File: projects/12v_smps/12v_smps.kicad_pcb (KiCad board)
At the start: 6 copper layers, 7 parts, among them U2 TPSM82902SISR

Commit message: wip
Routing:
- net /VIN: track 3.07 -> 0.00 mm
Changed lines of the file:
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@@
 		(property ki_fp_filters "R_*")
 		(sheetname "/")
+		(sheetfile "12v_smps.kicad_sch")
 		(attr smd)
 		(fp_line
@@
 		(property ki_fp_filters "uSIP11_SIS_TEX uSIP11_SIS_TEX-M uSIP11_SIS_TEX-L")
 		(sheetname "/")
+		(sheetfile "12v_smps.kicad_sch")
 		(attr smd)
 		(fp_line
@@
 		(property ki_fp_filters "R_*")
 		(sheetname "/")
+		(sheetfile "12v_smps.kicad_sch")
 		(attr smd dnp)
 		(fp_line
@@
 		(property ki_fp_filters "C_*")
 		(sheetname "/")
+		(sheetfile "12v_smps.kicad_sch")
 		(attr smd)
 		(fp_line
@@
 		(property ki_fp_filters "R_*")
 		(sheetname "/")
+		(sheetfile "12v_smps.kicad_sch")
 		(attr smd dnp)
 		(fp_line
@@
 		(property ki_fp_filters "C_*")
 		(sheetname "/")
+		(sheetfile "12v_smps.kicad_sch")
 		(attr smd dnp)
 		(fp_line
@@
 		(property ki_fp_filters "C_*")
 		(sheetname "/")
+		(sheetfile "12v_smps.kicad_sch")
 		(attr smd)
 		(fp_line
@@
 	)
 	(segment
-		(start 174.3459 60.262499)
-		(end 174.3459 60.899874)
-		(width 0.508)
-		(layer "F.Cu")
-		(net 3)
-	)
-	(segment
-		(start 174.3459 60.899874)
-		(end 174.3459 61.305426)
-		(width 0.508)
-		(layer "F.Cu")
-		(net 3)
-	)
-	(segment
-		(start 174.158401 60.075)
-		(end 174.3459 60.262499)
-		(width 0.508)
-		(layer "F.Cu")
-		(net 3)
-	)
-	(segment
-		(start 172.4 60.075)
-		(end 174.158401 60.075)
-		(width 0.508)
-		(layer "F.Cu")
-		(net 3)
-	)
-	(segment

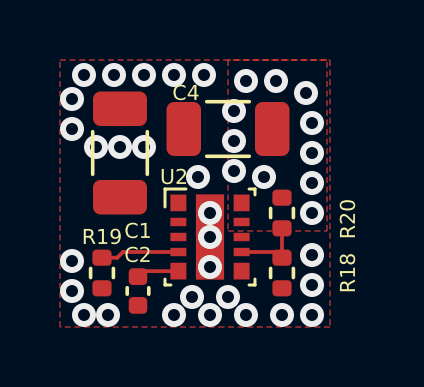
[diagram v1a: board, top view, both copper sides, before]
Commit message: 12v smps block
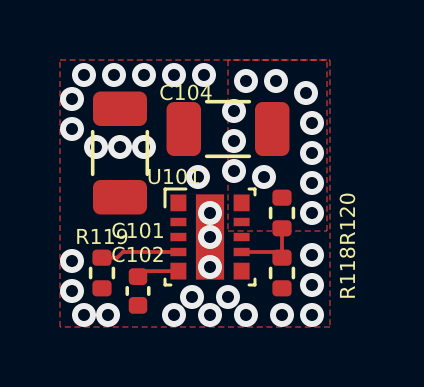
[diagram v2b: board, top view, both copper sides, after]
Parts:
- renumbered C1 to C101, C2 to C102, C4 to C104, R18 to R118, R19 to R119, R20 to R120, U2 to U101
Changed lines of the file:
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@@
 		(descr "Resistor SMD 0402 (1005 Metric), square (rectangular) end terminal, IPC-7351 nominal, (Body size source: IPC-SM-782 page 72, https://www.pcb-3d.com/wordpress/wp-content/uploads/ipc-sm-782a_amendment_1_and_2.pdf), generated with kicad-footprint-generator")
 		(tags "resistor")
-		(property "Reference" "R19"
+		(property "Reference" "R119"
 			(at -1.2 0 0)
 			(unlocked yes)
@@
 		(at 175.4 61.4)
 		(tags "TPSM82902SISR ")
-		(property "Reference" "U2"
+		(property "Reference" "U101"
 			(at -1.2 -2 0)
 			(unlocked yes)
@@
 		(descr "Resistor SMD 0402 (1005 Metric), square (rectangular) end terminal, IPC-7351 nominal, (Body size source: IPC-SM-782 page 72, https://www.pcb-3d.com/wordpress/wp-content/uploads/ipc-sm-782a_amendment_1_and_2.pdf), generated with kicad-footprint-generator")
 		(tags "resistor")
-		(property "Reference" "R20"
+		(property "Reference" "R120"
 			(at 0.2 -2.2 90)
 			(unlocked yes)
@@
 		(descr "Capacitor SMD 1206 (3216 Metric), square (rectangular) end terminal, IPC-7351 nominal, (Body size source: IPC-SM-782 page 76, https://www.pcb-3d.com/wordpress/wp-content/uploads/ipc-sm-782a_amendment_1_and_2.pdf), generated with kicad-footprint-generator")
 		(tags "capacitor")
-		(property "Reference" "C1"
+		(property "Reference" "C101"
 			(at -2.6 0.6 0)
 			(unlocked yes)
@@
 		(descr "Resistor SMD 0402 (1005 Metric), square (rectangular) end terminal, IPC-7351 nominal, (Body size source: IPC-SM-782 page 72, https://www.pcb-3d.com/wordpress/wp-content/uploads/ipc-sm-782a_amendment_1_and_2.pdf), generated with kicad-footprint-generator")
 		(tags "resistor")
-		(property "Reference" "R18"
+		(property "Reference" "R118"
 			(at 0 -2.2 90)
 			(unlocked yes)
@@
 		(descr "Capacitor SMD 0402 (1005 Metric), square (rectangular) end terminal, IPC-7351 nominal, (Body size source: IPC-SM-782 page 76, https://www.pcb-3d.com/wordpress/wp-content/uploads/ipc-sm-782a_amendment_1_and_2.pdf), generated with kicad-footprint-generator")
 		(tags "capacitor")
-		(property "Reference" "C2"
+		(property "Reference" "C102"
 			(at -1.2 0 0)
 			(unlocked yes)
@@
 		(descr "Capacitor SMD 1206 (3216 Metric), square (rectangular) end terminal, IPC-7351 nominal, (Body size source: IPC-SM-782 page 76, https://www.pcb-3d.com/wordpress/wp-content/uploads/ipc-sm-782a_amendment_1_and_2.pdf), generated with kicad-footprint-generator")
 		(tags "capacitor")
-		(property "Reference" "C4"
+		(property "Reference" "C104"
 			(at 1.4 1.2 0)
 			(unlocked yes)
